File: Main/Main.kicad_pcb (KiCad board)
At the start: 2 copper layers, 81.3 x 61 mm, 76 parts, among them J1 Conn_02x16_Odd_Even, J2 TYPE-C 6P, Q3 S9013 J3(RANGE:200-350), SW2 SS-12D11G3R, U1 BQ24074RGT, U2 DRV8833PW, U3 HUSB237-AA001-DN06R, U4 RT9742GGJ5, U5 RT9742GGJ5, U6 INA219AxDCN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

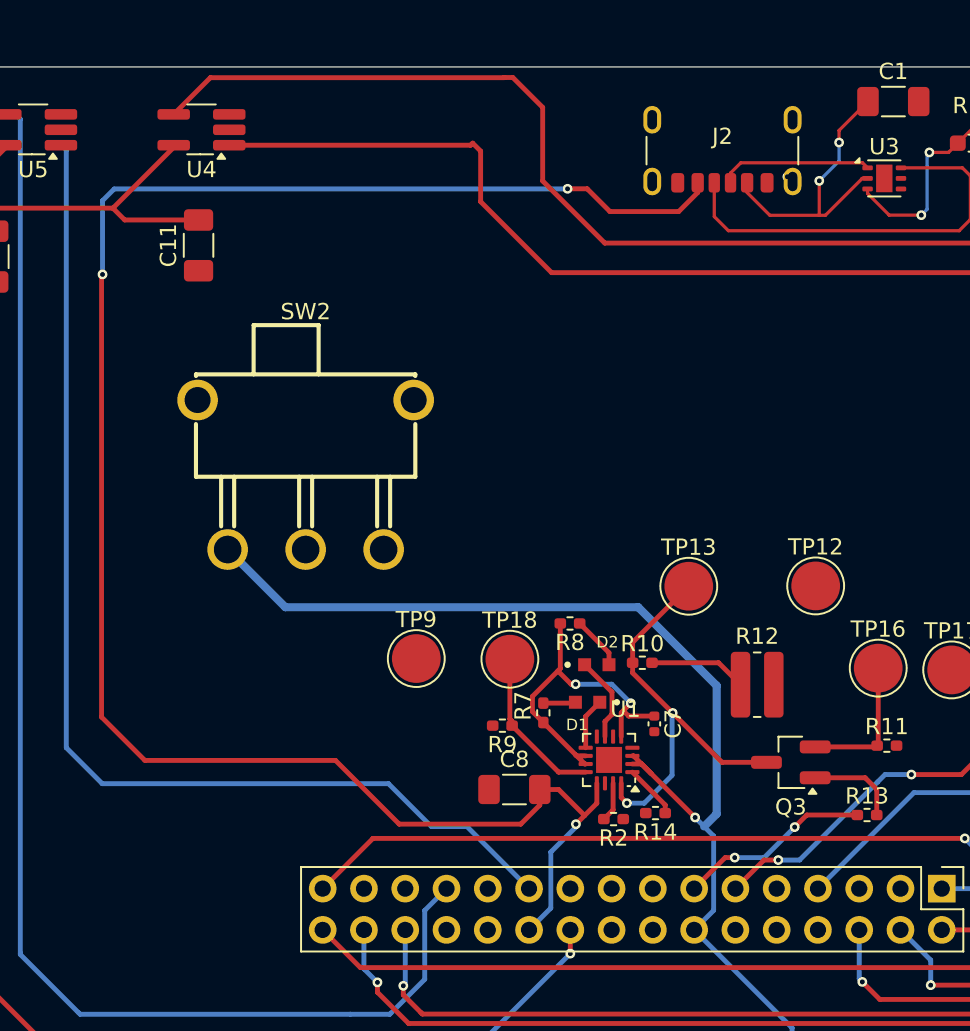
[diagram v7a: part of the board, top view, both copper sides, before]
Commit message: Changed all my 9V wires to 0,5mm
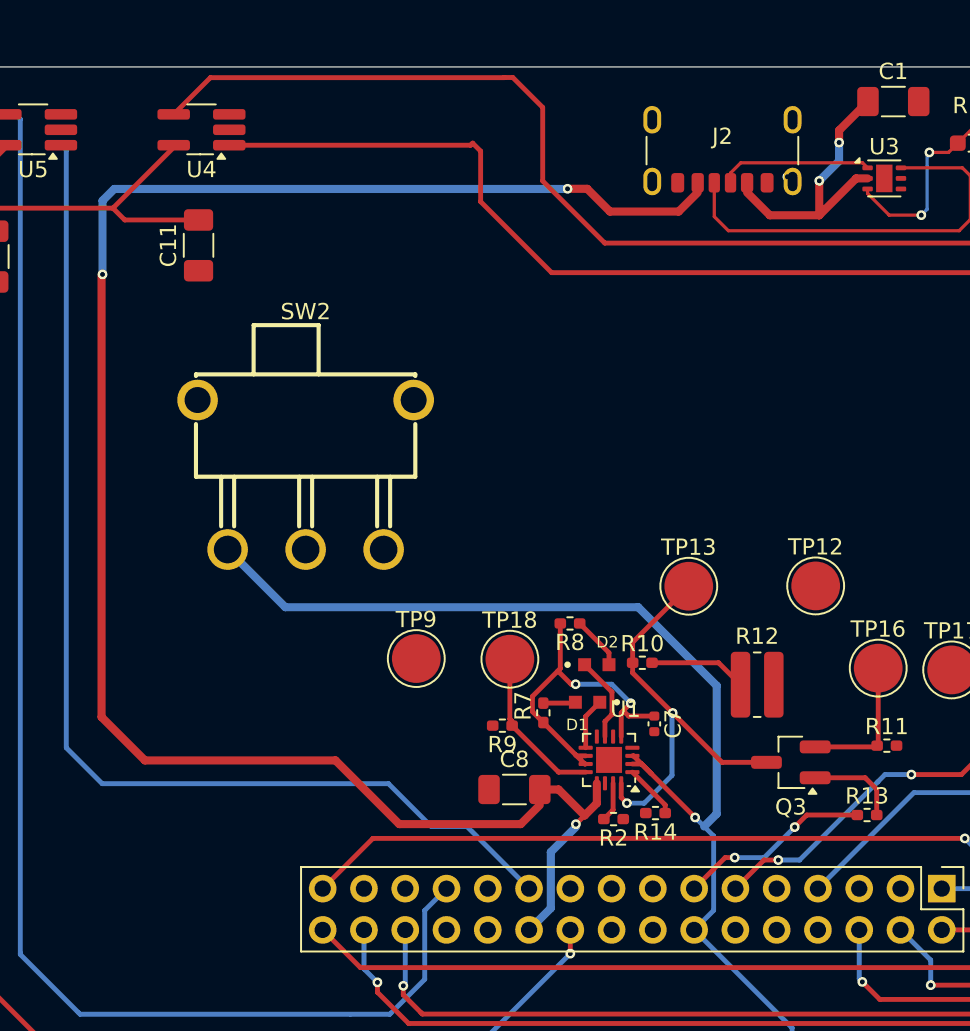
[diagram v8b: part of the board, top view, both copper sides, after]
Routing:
- net /High Voltage (9V): track 133.9 -> 133.0 mm
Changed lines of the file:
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@@
 		(start 129.47 97.4)
 		(end 121.99 97.4)
-		(width 0.3)
+		(width 0.5)
 		(layer "F.Cu")
 		(net 2)
@@
 		(start 132.35 58.3)
 		(end 133.56 58.3)
-		(width 0.3)
+		(width 0.5)
 		(layer "F.Cu")
 		(net 2)
@@
 		(start 149.06 55.45)
 		(end 149.06 54.7075)
-		(width 0.2)
+		(width 0.5)
 		(layer "F.Cu")
 		(net 2)
@@
 		(start 130.6425 96.2275)
 		(end 129.47 97.4)
-		(width 0.3)
+		(width 0.5)
 		(layer "F.Cu")
 		(net 2)
@@
 		(start 134.1525 96.1175)
 		(end 133.4 96.87)
-		(width 0.3)
+		(width 0.5)
 		(layer "F.Cu")
 		(net 2)
@@
 		(start 118.07 93.48)
 		(end 106.34 93.48)
-		(width 0.3)
-		(layer "F.Cu")
-		(net 2)
-	)
-	(segment
-		(start 150.815 57.66)
-		(end 150.47 57.66)
-		(width 0.2)
-		(layer "F.Cu")
-		(net 2)
-	)
-	(segment
-		(start 143.4 57.93)
-		(end 143.4 58.53)
-		(width 0.2)
+		(width 0.5)
 		(layer "F.Cu")
 		(net 2)
@@
 	)
 	(segment
-		(start 147.84 59.93)
-		(end 148.22 59.93)
-		(width 0.2)
+		(start 150.11 57.66)
+		(end 150.815 57.66)
+		(width 0.5)
 		(layer "F.Cu")
 		(net 2)
@@
 		(start 131.8 95.27)
 		(end 133.4 96.87)
-		(width 0.3)
+		(width 0.5)
 		(layer "F.Cu")
 		(net 2)
@@
 		(start 133.56 58.3)
 		(end 134.96 59.7)
-		(width 0.3)
+		(width 0.5)
 		(layer "F.Cu")
 		(net 2)
@@
 		(start 147.84 59.93)
 		(end 147.84 57.81)
-		(width 0.2)
+		(width 0.5)
+		(layer "F.Cu")
+		(net 2)
+	)
+	(segment
+		(start 147.84 59.93)
+		(end 150.11 57.66)
+		(width 0.5)
 		(layer "F.Cu")
 		(net 2)
@@
 		(start 103.67 90.81)
 		(end 103.67 63.63)
-		(width 0.3)
+		(width 0.5)
 		(layer "F.Cu")
 		(net 2)
@@
 		(start 106.34 93.48)
 		(end 103.67 90.81)
-		(width 0.3)
+		(width 0.5)
 		(layer "F.Cu")
 		(net 2)
@@
 		(start 134.1525 94.8875)
 		(end 134.1525 96.1175)
-		(width 0.3)
+		(width 0.5)
 		(layer "F.Cu")
 		(net 2)
@@
 		(start 144.8 59.93)
 		(end 147.84 59.93)
-		(width 0.2)
+		(width 0.5)
 		(layer "F.Cu")
 		(net 2)
@@
 		(start 130.6425 95.27)
 		(end 131.8 95.27)
-		(width 0.3)
+		(width 0.5)
 		(layer "F.Cu")
 		(net 2)
@@
 		(start 139.19 59.7)
 		(end 140.36 58.53)
-		(width 0.3)
+		(width 0.5)
 		(layer "F.Cu")
 		(net 2)
@@
 		(start 121.99 97.4)
 		(end 118.07 93.48)
-		(width 0.3)
+		(width 0.5)
 		(layer "F.Cu")
 		(net 2)
@@
 		(start 143.4 58.53)
 		(end 144.8 59.93)
-		(width 0.2)
+		(width 0.5)
 		(layer "F.Cu")
 		(net 2)
@@
 		(start 134.96 59.7)
 		(end 139.19 59.7)
-		(width 0.3)
-		(layer "F.Cu")
-		(net 2)
-	)
-	(segment
-		(start 150.49 57.66)
-		(end 150.815 57.66)
-		(width 0.2)
+		(width 0.5)
 		(layer "F.Cu")
 		(net 2)
@@
 		(start 149.06 54.7075)
 		(end 150.8375 52.93)
-		(width 0.2)
-		(layer "F.Cu")
-		(net 2)
-	)
-	(segment
-		(start 148.22 59.93)
-		(end 150.49 57.66)
-		(width 0.2)
+		(width 0.5)
 		(layer "F.Cu")
 		(net 2)
@@
 		(start 131.319 99.121)
 		(end 131.319 102.571)
-		(width 0.3)
+		(width 0.5)
 		(layer "B.Cu")
 		(net 2)
@@
 		(start 103.73 63.57)
 		(end 103.73 59.03)
-		(width 0.3)
+		(width 0.5)
 		(layer "B.Cu")
 		(net 2)
@@
 		(start 131.319 102.571)
 		(end 129.98 103.91)
-		(width 0.3)
+		(width 0.5)
 		(layer "B.Cu")
 		(net 2)
@@
 		(start 149.06 56.59)
 		(end 149.06 55.45)
-		(width 0.2)
+		(width 0.5)
 		(layer "B.Cu")
 		(net 2)
@@
 		(start 103.73 59.03)
 		(end 104.45 58.31)
-		(width 0.3)
+		(width 0.5)
 		(layer "B.Cu")
 		(net 2)
@@
 		(start 132.865 97.575)
 		(end 131.319 99.121)
-		(width 0.3)
+		(width 0.5)
 		(layer "B.Cu")
 		(net 2)
@@
 		(start 147.84 57.81)
 		(end 149.06 56.59)
-		(width 0.2)
+		(width 0.5)
 		(layer "B.Cu")
 		(net 2)
@@
 		(start 104.45 58.31)
 		(end 132.34 58.31)
-		(width 0.3)
-		(layer "B.Cu")
-		(net 2)
+		(width 0.5)
+		(layer "B.Cu")
+		(net 2)
